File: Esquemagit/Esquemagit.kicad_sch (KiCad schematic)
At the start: 0 parts

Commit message: feat: fase final del esquematico
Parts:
- added C1: 10uF, symbol Device:C
- added C2: 1uF, symbol Device:C
- added C3: 10nF, symbol Device:C
- added C4, C5: 100nF, symbol Device:C
- added D1: LED, LED_SMD:LED_01005_0402Metric, symbol Device:LED
- added MK1: Microphone_Condenser, symbol Device:Microphone_Condenser
- added R1: 10K, Resistor_SMD:R_0805_2012Metric, symbol Device:R
- added R10: R, symbol Device:R
- added R11: 150, symbol Device:R
- added R2: 1K, symbol Device:R
- added R3, R4: 10K, symbol Device:R
- added R5: 4.7K, symbol Device:R
- added R6: 2.2K, symbol Device:R
- added R7: 3.3K, symbol Device:R
- added R8: 100K, symbol Device:R
- added R9: 10k, symbol Device:R
- added TP1, TP2, TP3, TP4, TP5, TP6: TestPoint, TestPoint:TestPoint_Pad_D1.5mm, symbol Connector:TestPoint
- added U1: ESP32-WROOM-32, RF_Module:ESP32-WROOM-32, symbol RF_Module:ESP32-WROOM-32
- added U1: LM358, symbol Amplifier_Operational:LM358
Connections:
- new net: C2.2, R6.1, R7.1, R8.2
- new net: C3.2, R7.2
- new net: C1.1, MK1.2 (+), R1.2
- new net: C1.2, R2.1
- new net: D1.2 (A), R11.2
- new net: C2.1, R5.2, U1.1
- new net: R2.2, R5.1, U1.2 (-)
- new net +3.3V: TP2.1
- new net 3.3V: C4.1, C5.2, R1.1, R10.1, R3.1, R3.2, R4.1, R8.1, R9.2, U1.2 (VDD), U1.25 (IO0), U1.3 (+)
- new net BOOT: TP6.1
- new net EN: TP5.1
- new net GND: C3.1, C4.2, C5.1, D1.1 (K), MK1.1 (-), R10.2, R4.2, R6.2, R9.1, TP1.1, U1.1 (GND), U1.15 (GND), U1.3 (EN), U1.38 (GND), U1.39 (GND)
- new net LED_CTRL: R11.1, U1.24 (IO2)
- new net RX: TP4.1, U1.34 (RXD0/IO3)
- new net SDA: U1.33 (IO21)
- new net SLC: U1.36 (IO22)
- new net TX: TP3.1, U1.35 (TXD0/IO1)
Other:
- removed sheet Untitled Sheet

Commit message: feat inicio de pcb
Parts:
- C1, C2, C3, C4, C5: footprint (none) -> Capacitor_THT:C_Disc_D5.0mm_W2.5mm_P5.00mm
- MK1: footprint (none) -> Connector_PinHeader_2.54mm:PinHeader_1x02_P2.54mm_Horizontal
- R1: footprint Resistor_SMD:R_0805_2012Metric -> Resistor_THT:R_Axial_DIN0207_L6.3mm_D2.5mm_P7.62mm_Horizontal
- R10, R11, R3, R5, R6, R7, R8, R9: footprint (none) -> Resistor_THT:R_Axial_DIN0207_L6.3mm_D2.5mm_P7.62mm_Horizontal
- R4: footprint (none) -> R_Axial_DIN0207_L6.3mm_D2.5mm_P7.62mm_Horizontal
- U1: footprint (none) -> Package_DIP:DIP-8_W7.62mm
- renumbered U1 to U5
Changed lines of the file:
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@@
 			)
 		)
-		(property "Footprint" ""
+		(property "Footprint" "Capacitor_THT:C_Disc_D5.0mm_W2.5mm_P5.00mm"
 			(at 136.1948 54.61 0)
 			(hide yes)
@@
 			)
 		)
-		(property "Footprint" ""
+		(property "Footprint" "Resistor_THT:R_Axial_DIN0207_L6.3mm_D2.5mm_P7.62mm_Horizontal"
 			(at 210.82 72.898 90)
 			(hide yes)
@@
 			)
 		)
-		(property "Footprint" ""
+		(property "Footprint" "Connector_PinHeader_2.54mm:PinHeader_1x02_P2.54mm_Horizontal"
 			(at 82.55 71.12 90)
 			(hide yes)
@@
 			)
 		)
-		(property "Footprint" ""
+		(property "Footprint" "Resistor_THT:R_Axial_DIN0207_L6.3mm_D2.5mm_P7.62mm_Horizontal"
 			(at 201.422 60.96 90)
 			(hide yes)
@@
 			)
 		)
-		(property "Footprint" ""
+		(property "Footprint" "Resistor_THT:R_Axial_DIN0207_L6.3mm_D2.5mm_P7.62mm_Horizontal"
 			(at 145.288 33.02 90)
 			(hide yes)
@@
 		(in_pos_files yes)
 		(dnp no)
-		(property "Reference" "U1"
+		(property "Reference" "U5"
 			(at 169.7833 30.48 0)
 			(show_name no)
@@
 			(project "Esquemagit"
 				(path "/879299c0-e012-4d5e-97a2-28af80789ecc"
-					(reference "U1")
+					(reference "U5")
 					(unit 1)
 				)
@@
 			)
 		)
-		(property "Footprint" ""
+		(property "Footprint" "Resistor_THT:R_Axial_DIN0207_L6.3mm_D2.5mm_P7.62mm_Horizontal"
 			(at 188.722 49.53 90)
 			(hide yes)
@@
 			)
 		)
-		(property "Footprint" ""
+		(property "Footprint" "R_Axial_DIN0207_L6.3mm_D2.5mm_P7.62mm_Horizontal"
 			(at 113.792 87.63 90)
 			(hide yes)
@@
 			)
 		)
-		(property "Footprint" ""
+		(property "Footprint" "Capacitor_THT:C_Disc_D5.0mm_W2.5mm_P5.00mm"
 			(at 65.7352 72.39 0)
 			(hide yes)
@@
 			)
 		)
-		(property "Footprint" ""
+		(property "Footprint" "Resistor_THT:R_Axial_DIN0207_L6.3mm_D2.5mm_P7.62mm_Horizontal"
 			(at 201.422 80.01 90)
 			(hide yes)
@@
 			)
 		)
-		(property "Footprint" ""
+		(property "Footprint" "Capacitor_THT:C_Disc_D5.0mm_W2.5mm_P5.00mm"
 			(at 96.52 67.6148 0)
 			(hide yes)
@@
 			)
 		)
-		(property "Footprint" ""
+		(property "Footprint" "Capacitor_THT:C_Disc_D5.0mm_W2.5mm_P5.00mm"
 			(at 217.4748 76.2 0)
 			(hide yes)
@@
 			)
 		)
-		(property "Footprint" ""
+		(property "Footprint" "Resistor_THT:R_Axial_DIN0207_L6.3mm_D2.5mm_P7.62mm_Horizontal"
 			(at 113.792 55.88 90)
 			(hide yes)
@@
 			)
 		)
-		(property "Footprint" ""
+		(property "Footprint" "Resistor_THT:R_Axial_DIN0207_L6.3mm_D2.5mm_P7.62mm_Horizontal"
 			(at 212.09 42.418 90)
 			(hide yes)
@@
 			)
 		)
-		(property "Footprint" ""
+		(property "Footprint" "Capacitor_THT:C_Disc_D5.0mm_W2.5mm_P5.00mm"
 			(at 201.93 70.1548 0)
 			(hide yes)
@@
 			)
 		)
-		(property "Footprint" "Resistor_SMD:R_0805_2012Metric"
+		(property "Footprint" "Resistor_THT:R_Axial_DIN0207_L6.3mm_D2.5mm_P7.62mm_Horizontal"
 			(at 80.772 55.88 90)
 			(hide yes)
@@
 			)
 		)
-		(property "Footprint" ""
+		(property "Footprint" "Resistor_THT:R_Axial_DIN0207_L6.3mm_D2.5mm_P7.62mm_Horizontal"
 			(at 125.73 84.328 90)
 			(hide yes)
@@
 			)
 		)
-		(property "Footprint" ""
+		(property "Footprint" "Package_DIP:DIP-8_W7.62mm"
 			(at 127 71.12 0)
 			(hide yes)

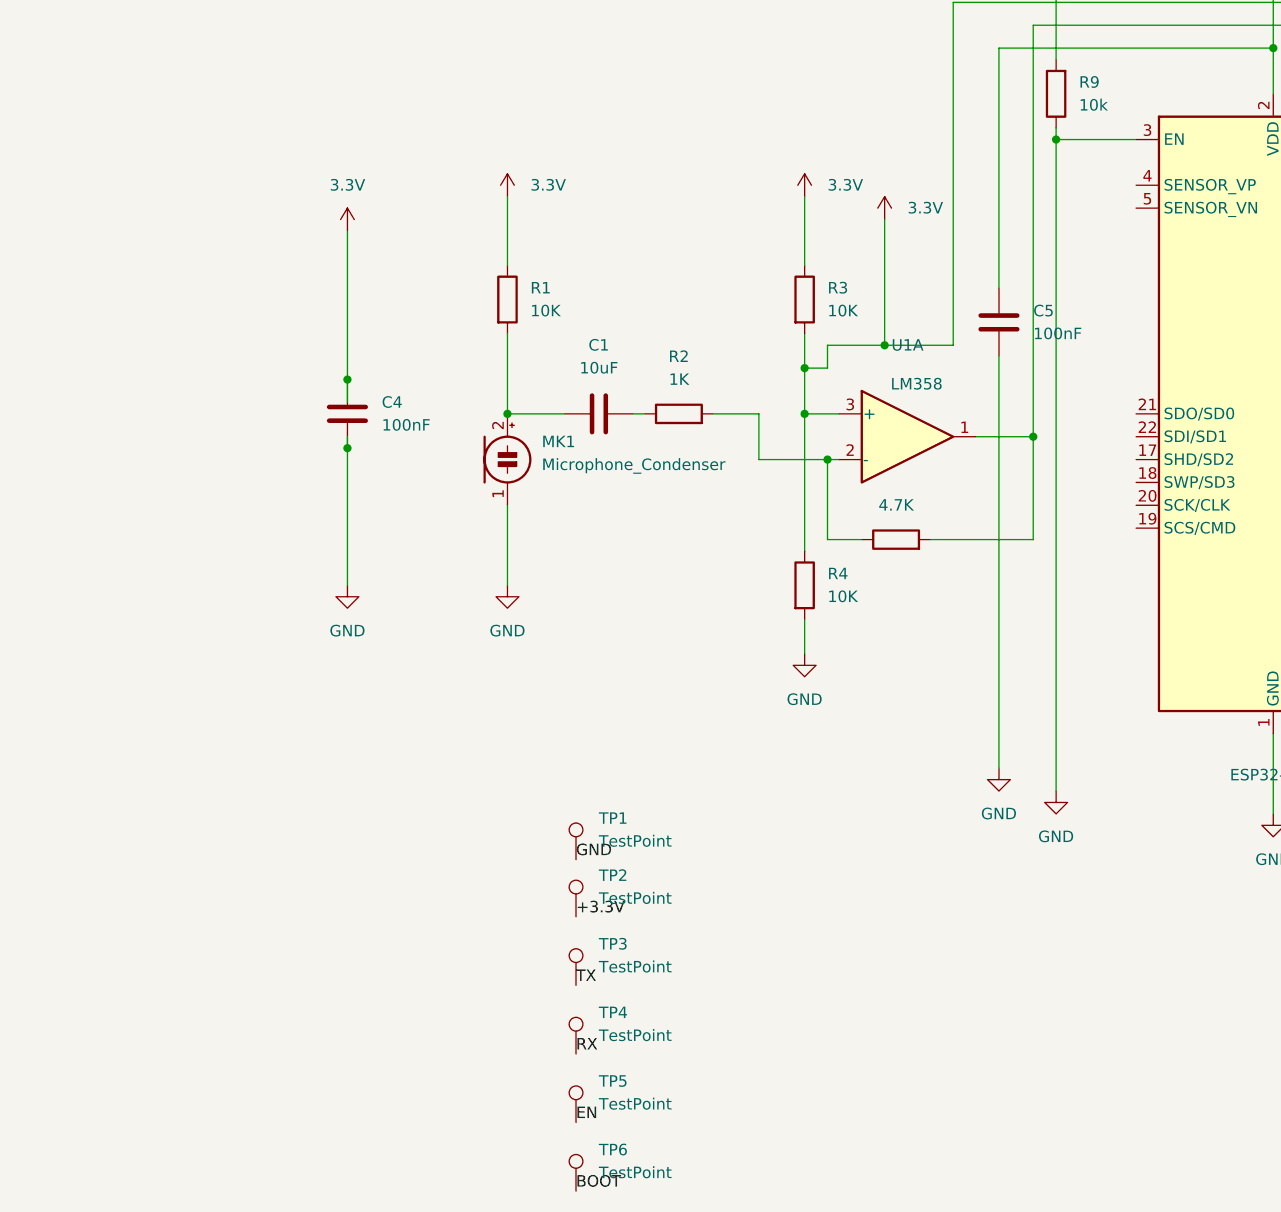
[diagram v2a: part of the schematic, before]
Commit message: Se agrego huellas, se realizo avances en la etapa de amplificacion en la pcb
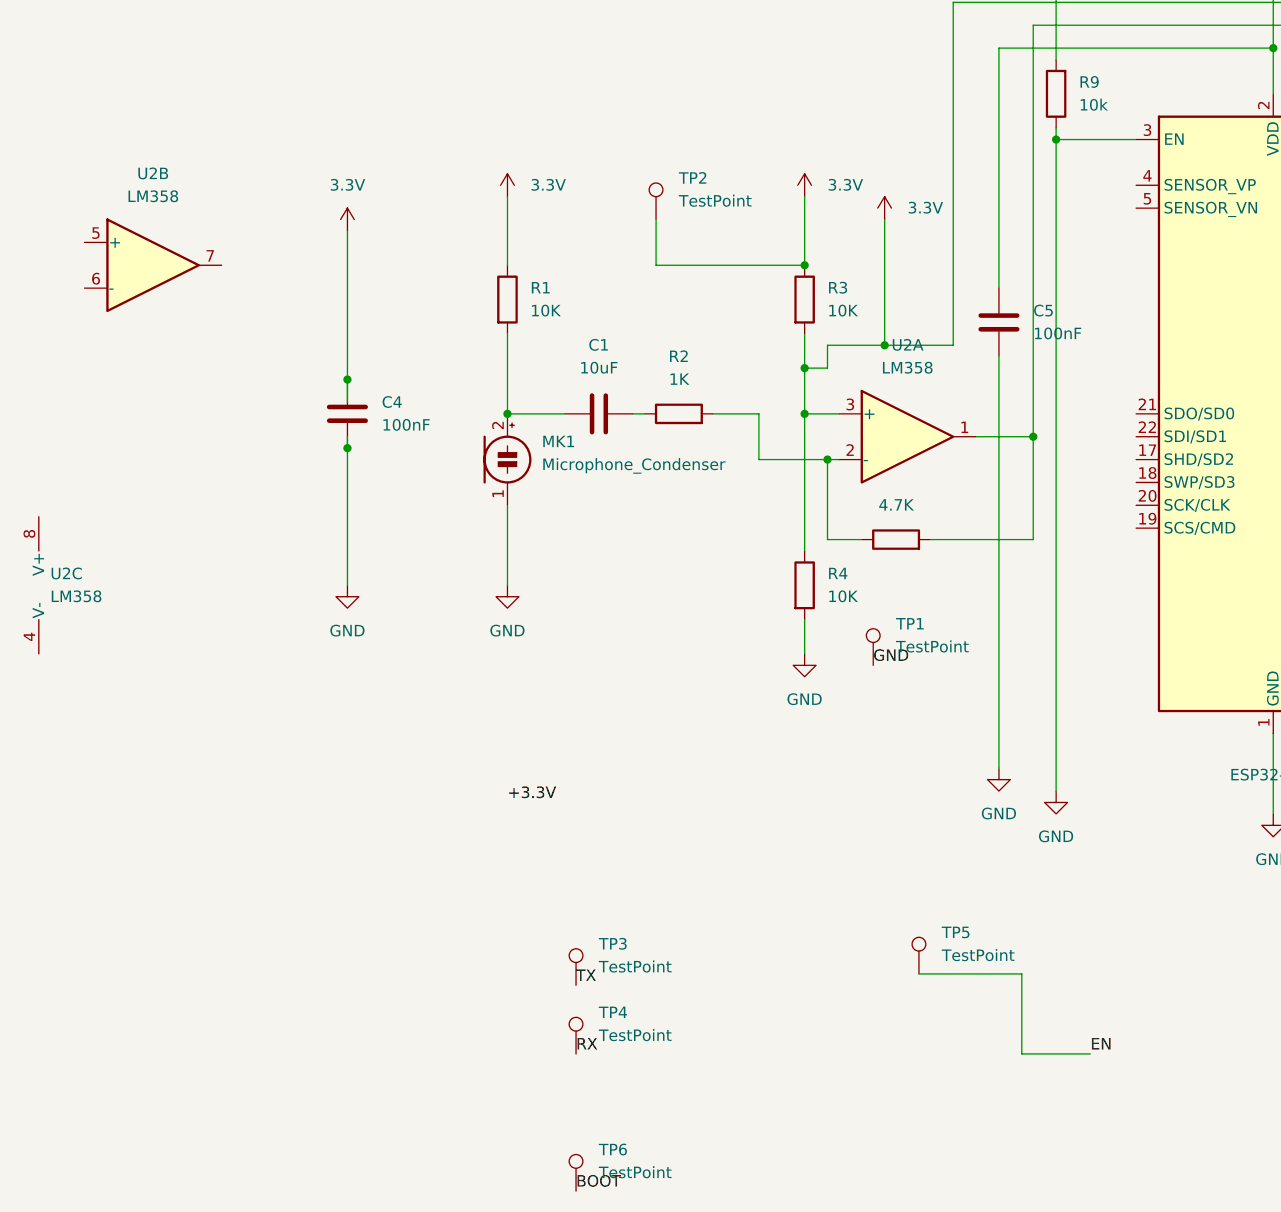
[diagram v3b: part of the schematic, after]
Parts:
- removed U1: LM358, Package_DIP:DIP-8_W7.62mm, symbol Amplifier_Operational:LM358
- added U2: LM358, Package_DIP:DIP-8_W7.62mm_Socket, symbol Amplifier_Operational:LM358
- R2: footprint (none) -> Resistor_THT:R_Axial_DIN0207_L6.3mm_D2.5mm_P7.62mm_Horizontal
- TP1, TP2, TP3, TP4, TP5, TP6: footprint TestPoint:TestPoint_Pad_D1.5mm -> TestPoint:TestPoint_Loop_D2.54mm_Drill1.5mm_Beaded
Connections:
- net +3.3V: no longer TP2.1
- net 3.3V: now also TP2.1, U2.3 (+)
- net at C2.1, R5.2: now also U2.1
- net at R2.2, R5.1: now also U2.2 (-)
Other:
- moved on the sheet: TP1, TP2, TP5

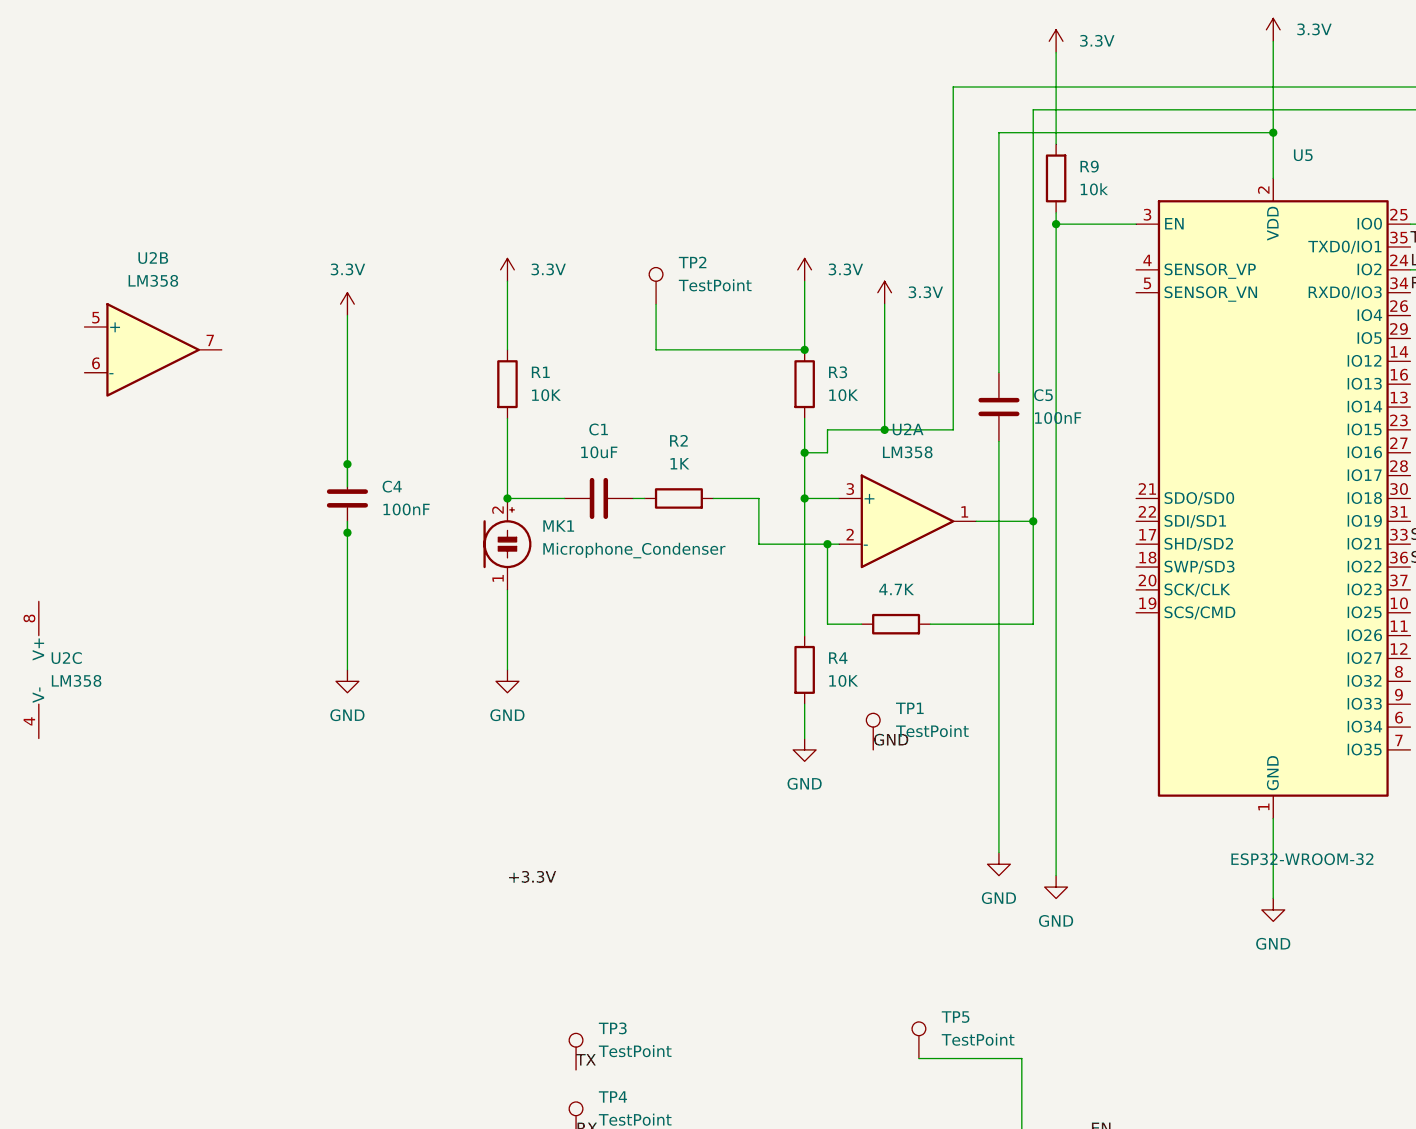
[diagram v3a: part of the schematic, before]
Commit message: feat: actualizaciones en el diseño del esquematico
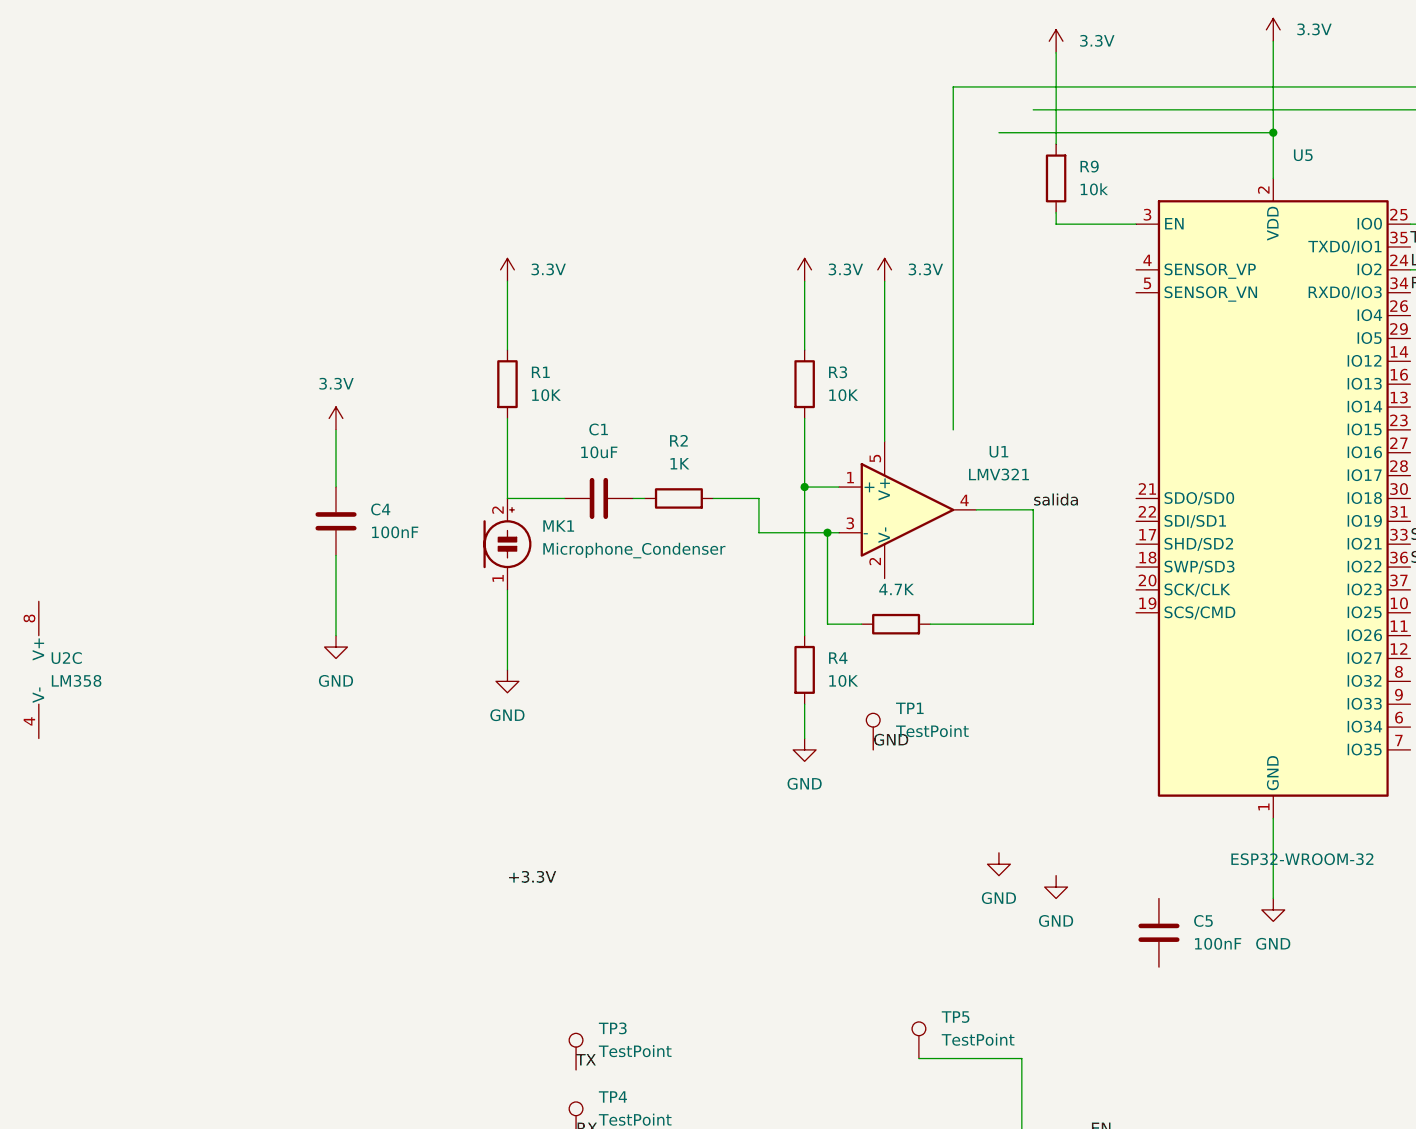
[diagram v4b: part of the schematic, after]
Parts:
- removed TP2: TestPoint, TestPoint:TestPoint_Loop_D2.54mm_Drill1.5mm_Beaded, symbol Connector:TestPoint
- removed unit 2 of U2
- removed unit 1 of U2
- added U1: LMV321, Package_TO_SOT_SMD:SOT-23-5_HandSoldering, symbol Amplifier_Operational:LMV321
- C1: footprint Capacitor_THT:C_Disc_D5.0mm_W2.5mm_P5.00mm -> Capacitor_SMD:C_0805_2012Metric
- R1, R2, R5: footprint Resistor_THT:R_Axial_DIN0207_L6.3mm_D2.5mm_P7.62mm_Horizontal -> Resistor_SMD:R_0805_2012Metric
- R4: footprint R_Axial_DIN0207_L6.3mm_D2.5mm_P7.62mm_Horizontal -> Resistor_SMD:R_0805_2012Metric
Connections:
- net 3.3V: now also U1.5 (V+); no longer C5.2, R3.2, R4.1, R8.1
- net GND: no longer C5.1, R9.1, U5.3 (EN)
- net at C2.1: no longer R5.2
- net at R2.2, R5.1: now also U1.3 (-)
- new net: R9.1, U5.3 (EN)
- new net: R3.2, R4.1, U1.1 (+)
- new net salida: R5.2, U1.4
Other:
- moved on the sheet: C4, C5

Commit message: feat: actualizaciones en el diseño 2
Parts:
- removed TP1, TP3, TP4, TP5, TP6: TestPoint, TestPoint:TestPoint_Loop_D2.54mm_Drill1.5mm_Beaded, symbol Connector:TestPoint
- removed U2: LM358, Package_DIP:DIP-8_W7.62mm_Socket, symbol Amplifier_Operational:LM358
- C2, C3, C5: footprint Capacitor_THT:C_Disc_D5.0mm_W2.5mm_P5.00mm -> Capacitor_SMD:C_0805_2012Metric
- D1: footprint LED_SMD:LED_01005_0402Metric -> LED_SMD:LED_0805_2012Metric
- R10: value R -> 10; footprint Resistor_THT:R_Axial_DIN0207_L6.3mm_D2.5mm_P7.62mm_Horizontal -> Resistor_SMD:R_0805_2012Metric
- R11, R6, R7, R8, R9: footprint Resistor_THT:R_Axial_DIN0207_L6.3mm_D2.5mm_P7.62mm_Horizontal -> Resistor_SMD:R_0805_2012Metric
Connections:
- net 3.3V: now also C5.2, R8.1; no longer U5.25 (IO0)
- net GND: now also C5.1; no longer R10.2
- net LED_CTRL: now also R11.2; no longer R11.1
- net salida: now also C2.1
- net at D1.2 (A): now also R11.1; no longer R11.2
- new net: R10.2, U5.25 (IO0)
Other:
- note added: "Etapa de Audio"
- note added: "capacitarores de desacople"
- note added: "filtro de salida"
- moved on the sheet: C1, C2, C3, C4, C5, D1, MK1, R1, R10, R11, R2, R3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
